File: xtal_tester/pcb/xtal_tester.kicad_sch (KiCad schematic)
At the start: 20 parts, among them J1 Conn_01x04, J2 Conn_01x04, J3 Conn_01x04, Q1 Q_NPN_ECB, Q2 Q_NPN_ECB, Y1 Crystal

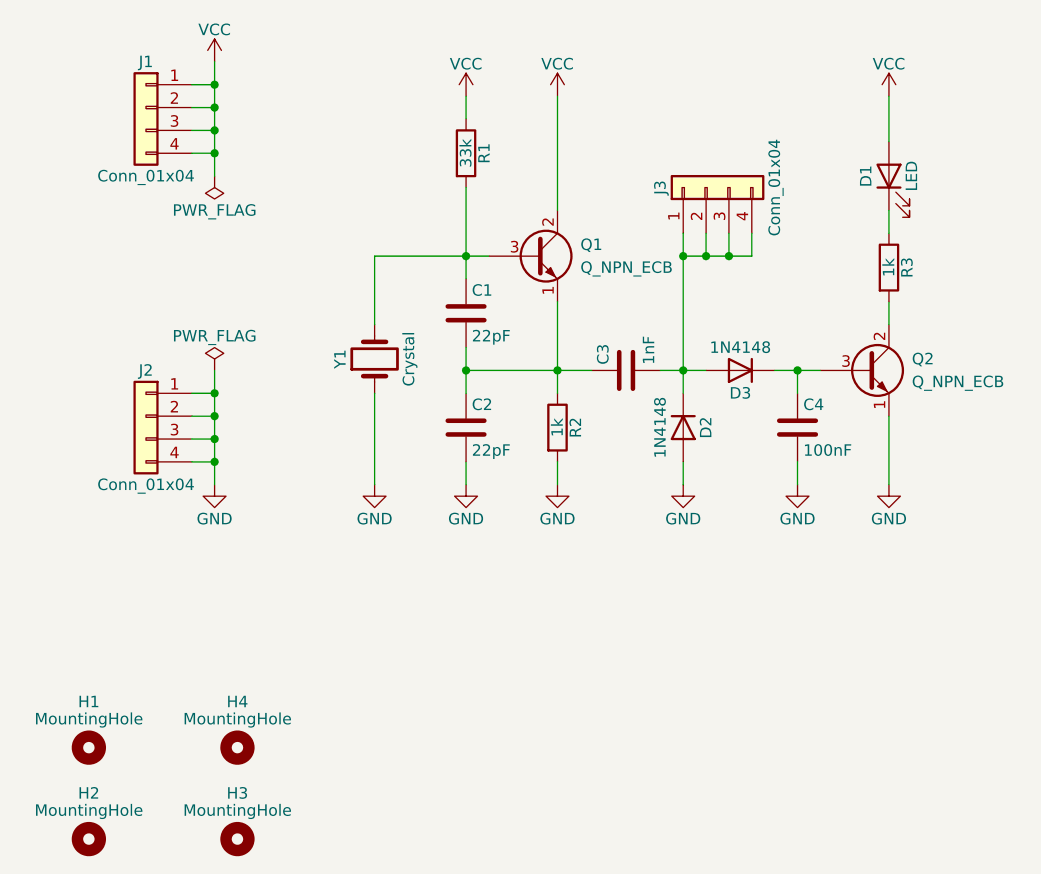
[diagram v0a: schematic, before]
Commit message: change xtal footprint to pin header
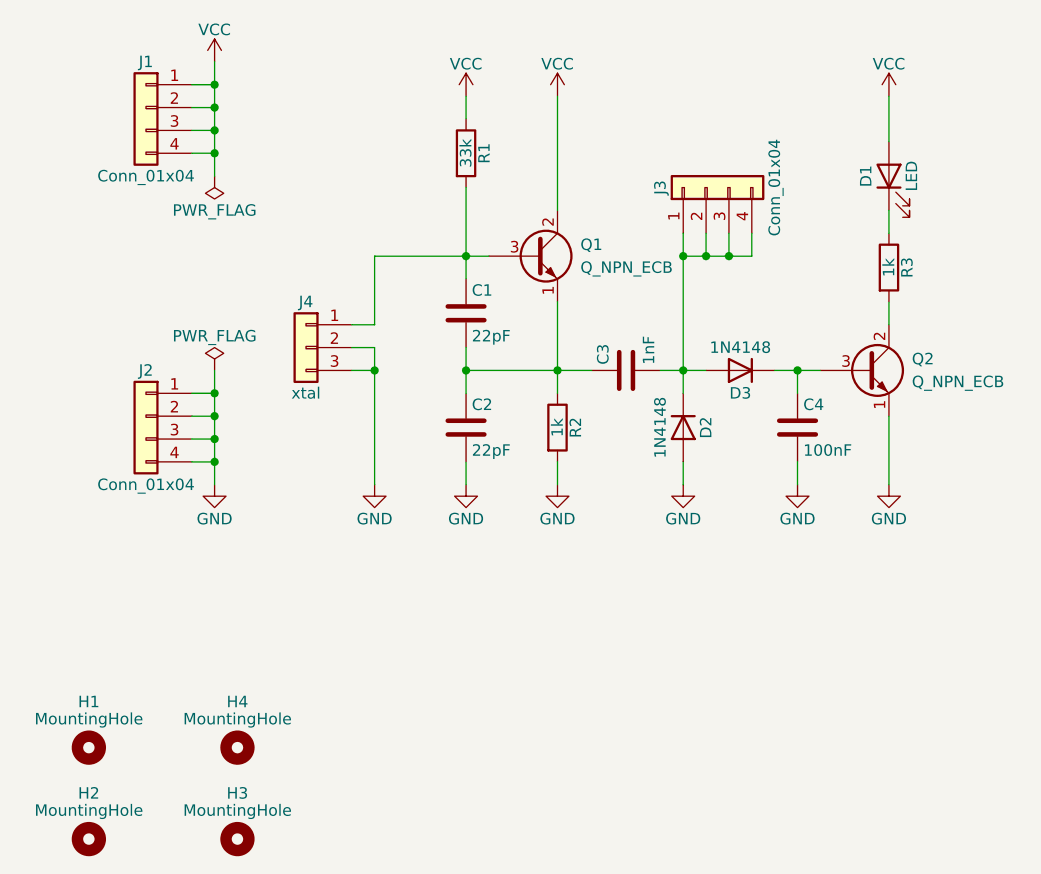
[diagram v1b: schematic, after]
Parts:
- removed Y1: Crystal, Crystal:Crystal_HC18-U_Vertical, symbol Device:Crystal
- added J4: xtal, Connector_PinHeader_2.54mm:PinHeader_1x03_P2.54mm_Vertical, symbol Connector_Generic:Conn_01x03
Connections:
- net GND: now also J4.2 (Pin_2), J4.3 (Pin_3)
- net at C1.1, Q1.3 (B), R1.2: now also J4.1 (Pin_1)
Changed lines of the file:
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@@
+	)
+	(junction
+		(at 113.03 92.71)
+		(diameter 0)
+		(color 0 0 0 0)
 	)
 	(junction
@@
 	(wire
 		(pts
+			(xy 113.03 92.71) (xy 113.03 105.41)
+		)
+		(stroke
+			(width 0)
+			(type default)
+		)
+	)
+	(wire
+		(pts
 			(xy 152.4 77.47) (xy 152.4 80.01)
 		)
@@
 	(wire
 		(pts
+			(xy 113.03 90.17) (xy 110.49 90.17)
+		)
+		(stroke
+			(width 0)
+			(type default)
+		)
+	)
+	(wire
+		(pts
 			(xy 95.25 102.87) (xy 95.25 100.33)
 		)
@@
 	(wire
 		(pts
+			(xy 113.03 90.17) (xy 113.03 92.71)
+		)
+		(stroke
+			(width 0)
+			(type default)
+		)
+	)
+	(wire
+		(pts
 			(xy 160.02 92.71) (xy 162.56 92.71)
 		)
@@
 	(wire
 		(pts
+			(xy 110.49 92.71) (xy 113.03 92.71)
+		)
+		(stroke
+			(width 0)
+			(type default)
+		)
+	)
+	(wire
+		(pts
 			(xy 95.25 58.42) (xy 95.25 60.96)
 		)
@@
 	(wire
 		(pts
-			(xy 113.03 95.25) (xy 113.03 105.41)
-		)
-		(stroke
-			(width 0)
-			(type default)
-		)
-	)
-	(wire
-		(pts
 			(xy 95.25 95.25) (xy 92.71 95.25)
 		)
@@
 	(wire
 		(pts
+			(xy 110.49 87.63) (xy 113.03 87.63)
+		)
+		(stroke
+			(width 0)
+			(type default)
+		)
+	)
+	(wire
+		(pts
 			(xy 147.32 92.71) (xy 149.86 92.71)
 		)
@@
 	)
 	(symbol
-		(lib_id "Device:Crystal")
-		(at 113.03 91.44 90)
+		(lib_id "Connector_Generic:Conn_01x03")
+		(at 105.41 90.17 0)
+		(mirror y)
 		(unit 1)
 		(exclude_from_sim no)
@@
 		(on_board yes)
 		(dnp no)
-		(property "Reference" "Y1"
-			(at 109.22 91.44 0)
+		(property "Reference" "J4"
+			(at 105.41 85.09 0)
 			(effects
 				(font
@@
 			)
 		)
-		(property "Value" "Crystal"
-			(at 116.84 91.44 0)
+		(property "Value" "xtal"
+			(at 105.41 95.25 0)
 			(effects
 				(font
@@
 			)
 		)
-		(property "Footprint" "Crystal:Crystal_HC18-U_Vertical"
-			(at 113.03 91.44 0)
+		(property "Footprint" "Connector_PinHeader_2.54mm:PinHeader_1x03_P2.54mm_Vertical"
+			(at 105.41 90.17 0)
 			(effects
 				(font
@@
 		)
 		(property "Datasheet" "~"
-			(at 113.03 91.44 0)
+			(at 105.41 90.17 0)
 			(effects
 				(font
@@
 			)
 		)
-		(property "Description" "Two pin crystal"
-			(at 113.03 91.44 0)
+		(property "Description" "Generic connector, single row, 01x03, script generated (kicad-library-utils/schlib/autogen/connector/)"
+			(at 105.41 90.17 0)
 			(effects
 				(font
@@
 			)
 		)
+		(pin "3"
+		)
+		(pin "2"
+		)
 		(pin "1"
-		)
-		(pin "2"
 		)
 		(instances
 			(project "xtal_tester"
 				(path "/04652f35-f7e2-426d-bd1a-7e46a12e493a"
-					(reference "Y1")
+					(reference "J4")
 					(unit 1)
 				)
